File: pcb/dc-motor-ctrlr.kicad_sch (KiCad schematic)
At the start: 17 parts, among them U1 TPS5450, U2 LP2985-3.3

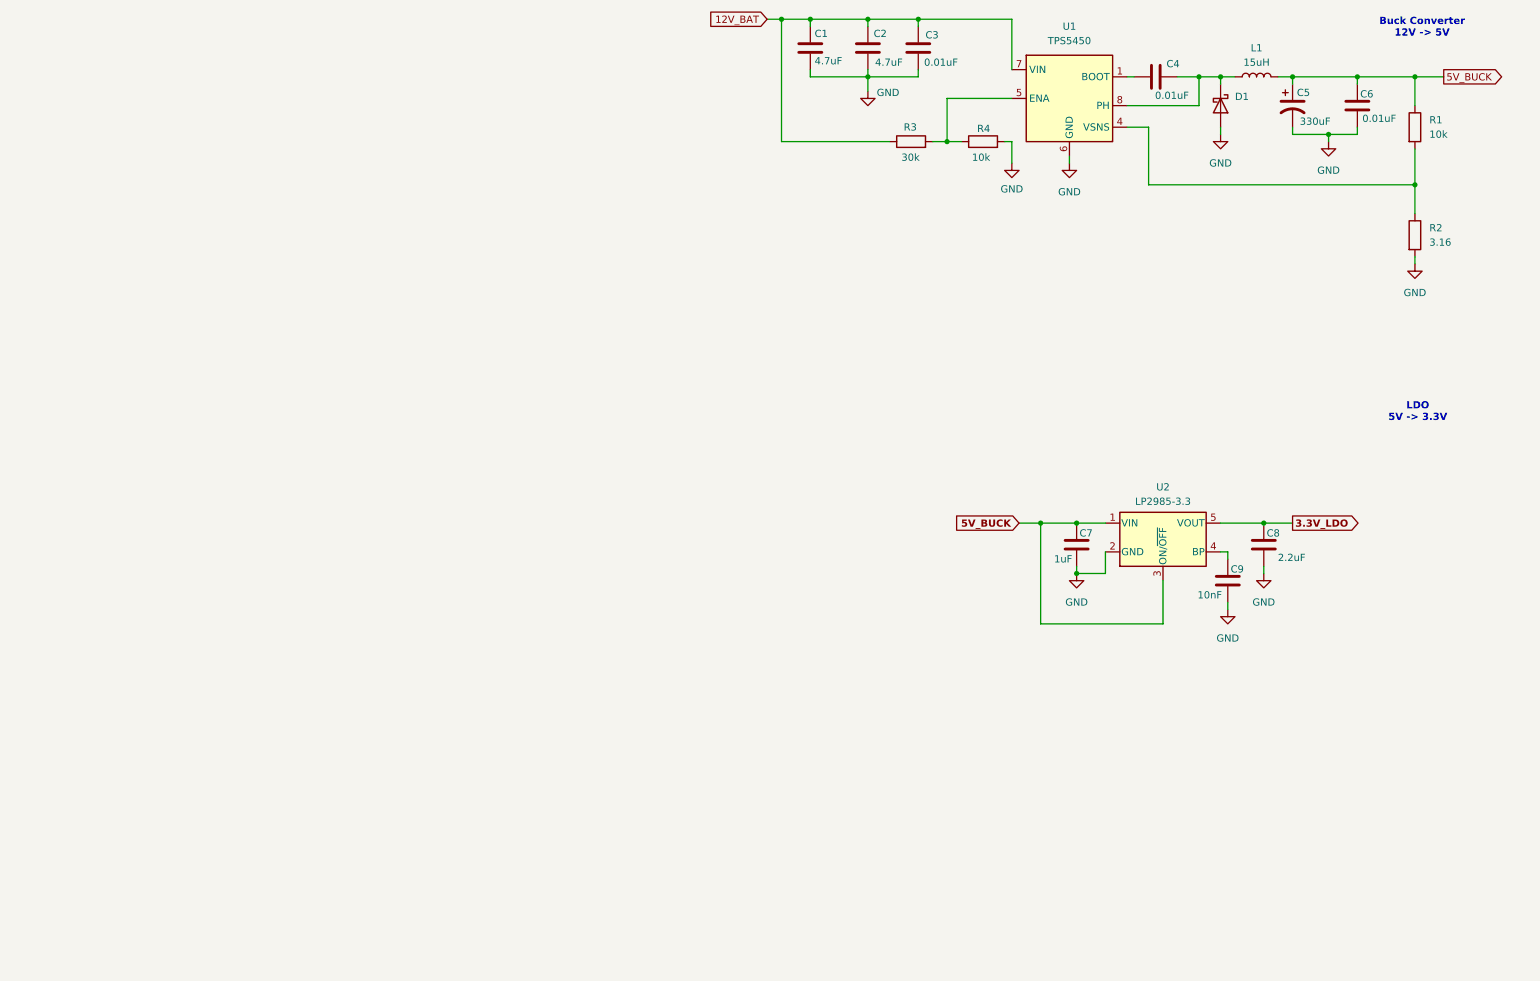
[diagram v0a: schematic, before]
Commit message: added battery connectors and DC jack
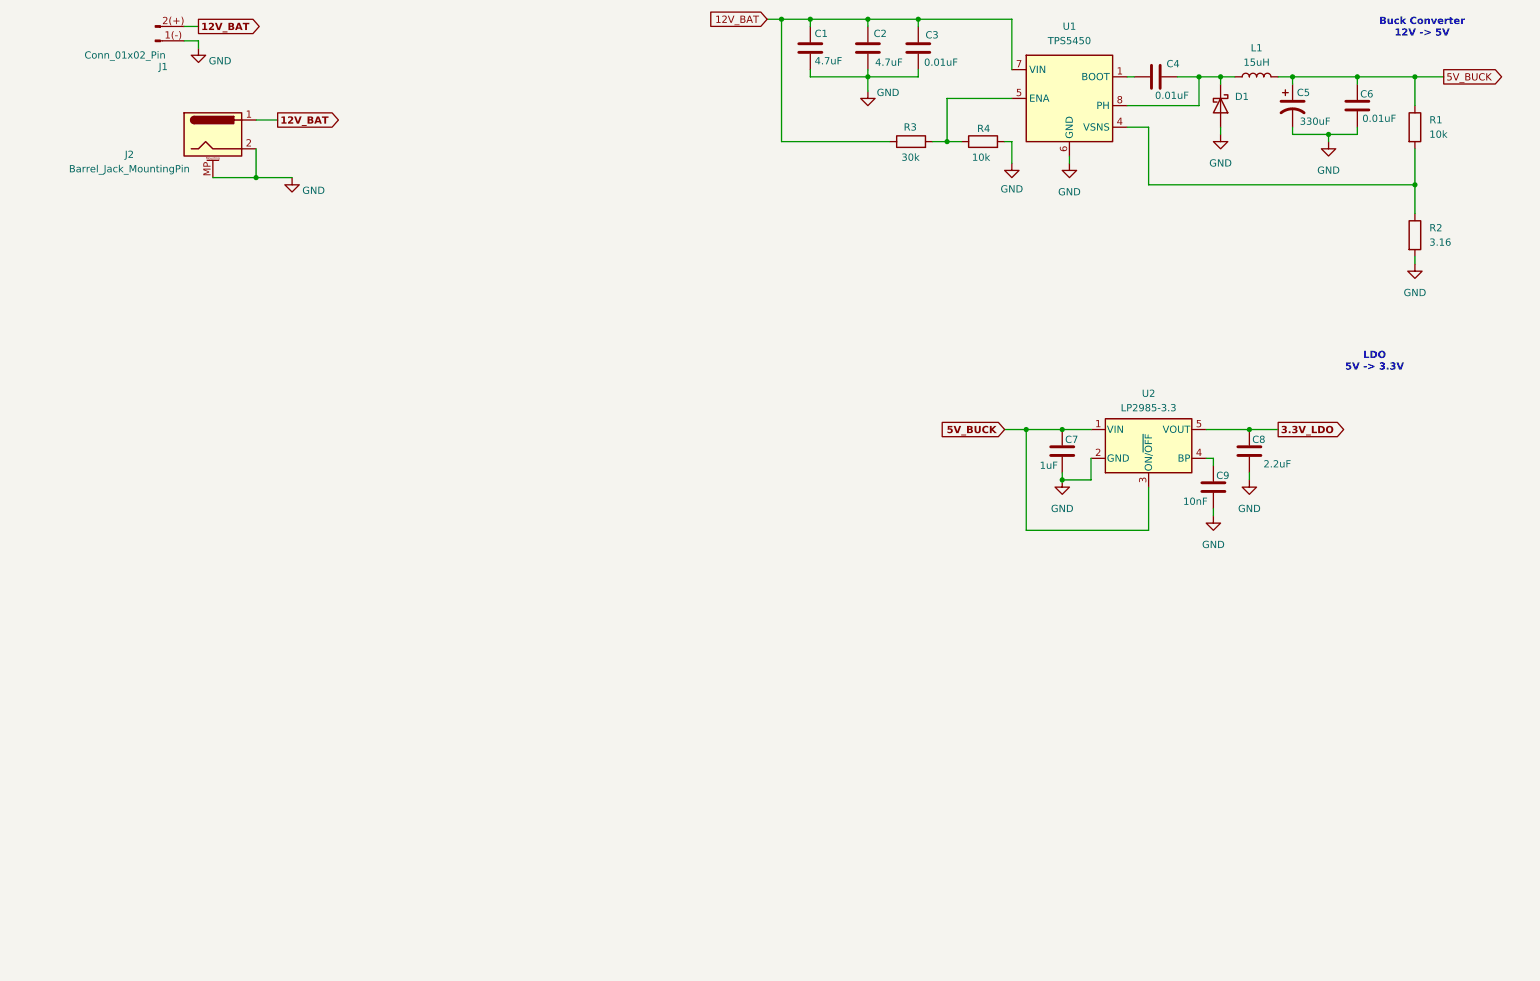
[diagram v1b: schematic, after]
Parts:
- added J1: Conn_01x02_Pin, AMASS_XT60IPW-M_1x03_P7.20mm_Horizontal, symbol Connector:Conn_01x02_Pin
- added J2: Barrel_Jack_MountingPin, symbol Connector:Barrel_Jack_MountingPin
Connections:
- net 12V_BAT: now also J1.2(+) (Pin_2), J2.1
- net GND: now also J1.1(-) (Pin_1), J2.2, J2.MP (MountPin)
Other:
- moved on the sheet: C7, C8, C9, U2

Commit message: Added motor driver
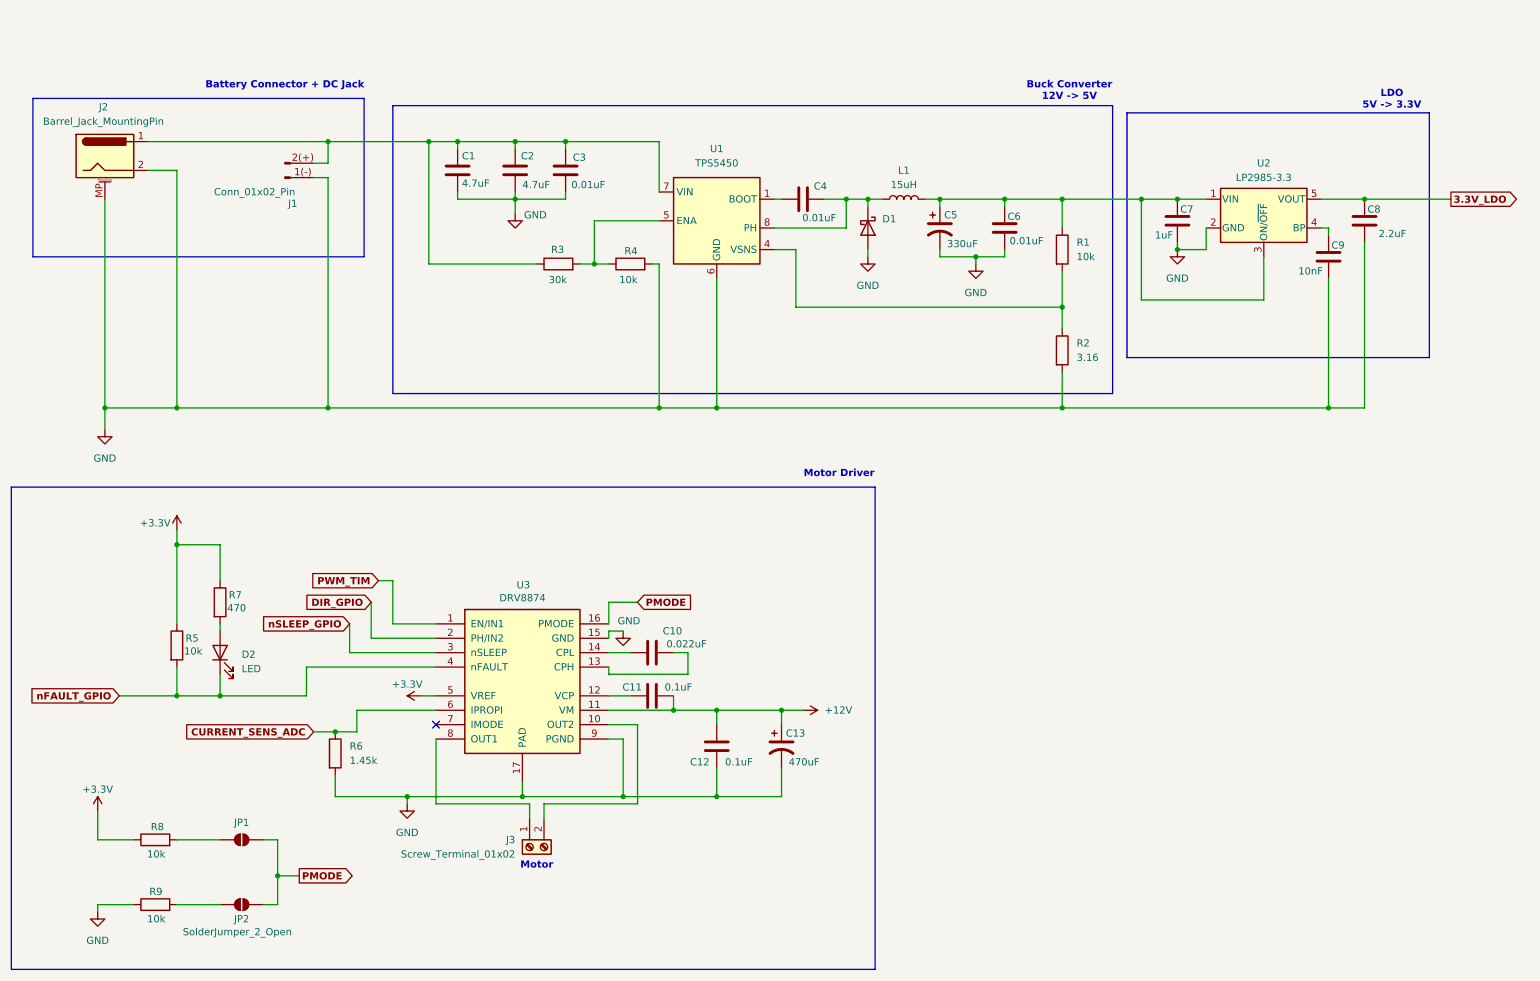
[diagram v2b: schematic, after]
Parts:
- added C10: 0.022uF, symbol Device:C
- added C11, C12: 0.1uF, symbol Device:C
- added C13: 470uF, symbol Device:C_Polarized_US
- added D2: LED, symbol Device:LED
- added J3: Screw_Terminal_01x02, symbol Connector:Screw_Terminal_01x02
- added JP1, JP2: SolderJumper_2_Open, symbol Jumper:SolderJumper_2_Open
- added R5, R8, R9: 10k, symbol Device:R
- added R6: 1.45k, symbol Device:R
- added R7: 470, symbol Device:R
- added U3: DRV8874, HTSSOP-16-1EP_4.4x5mm_P0.65mm_EP3.4x5mm_Mask2.46x2.31mm_ThermalVias, symbol Driver_Motor:DRV8833PWP
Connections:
- net GND: now also C12.1, C13.2, R6.2, R9.1, U3.15 (GND), U3.17 (PAD), U3.9 (PGND)
- net 12V_BAT: no longer names the net of C1.1, C2.1, C3.1, J1.2(+) (Pin_2), J2.1, R3.1, U1.7 (VIN)
- net 5V_BUCK: no longer names the net of C5.1, C6.2, C7.2, L1.2, R1.1, U2.1 (VIN), U2.3 (ON/~{OFF})
- new net: JP2.1 (A), R9.2
- new net: JP1.1 (A), R8.2
- new net: C11.1, U3.12 (VCP)
- new net: C10.1, U3.14 (CPL)
- new net: C10.2, U3.13 (CPH)
- new net: D2.2 (A), R7.2
- new net: J3.2 (Pin_2), U3.10 (OUT2)
- new net: J3.1 (Pin_1), U3.8 (OUT1)
- new net +12V: C11.2, C12.2, C13.1, U3.11 (VM)
- new net +3.3V: R5.1, R7.1, R8.1, U3.5 (VREF)
- new net CURRENT_SENS_ADC: R6.1, U3.6 (IPROPI)
- new net DIR_GPIO: U3.2 (PH/IN2)
- new net PMODE: JP1.2 (B), JP2.2 (B), U3.16 (PMODE)
- new net PWM_TIM: U3.1 (EN/IN1)
- new net nFAULT_GPIO: D2.1 (K), R5.2, U3.4 (nFAULT)
- new net nSLEEP_GPIO: U3.3 (nSLEEP)
- no-connect marks 0 -> 1
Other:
- note added: "Battery Connector + DC Jack"
- note added: "Motor"
- note added: "Motor Driver"
- moved on the sheet: C1, C2, C3, C4, C5, C6, C7, C8, C9, D1, J1, J2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
